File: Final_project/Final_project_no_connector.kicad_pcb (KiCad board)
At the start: 2 copper layers, 66 x 34.6 mm, 56 parts, among them J1 USB4105-GF-A, J2 Conn_01x04, J4 LEFT, J5 RIGHT, U1 RP2040, U2 MCP1702T-3302E_CB, U3 W25Q128JV, U4 ESP32-WROOM-32, U5 LM393D, Y1 12MHz

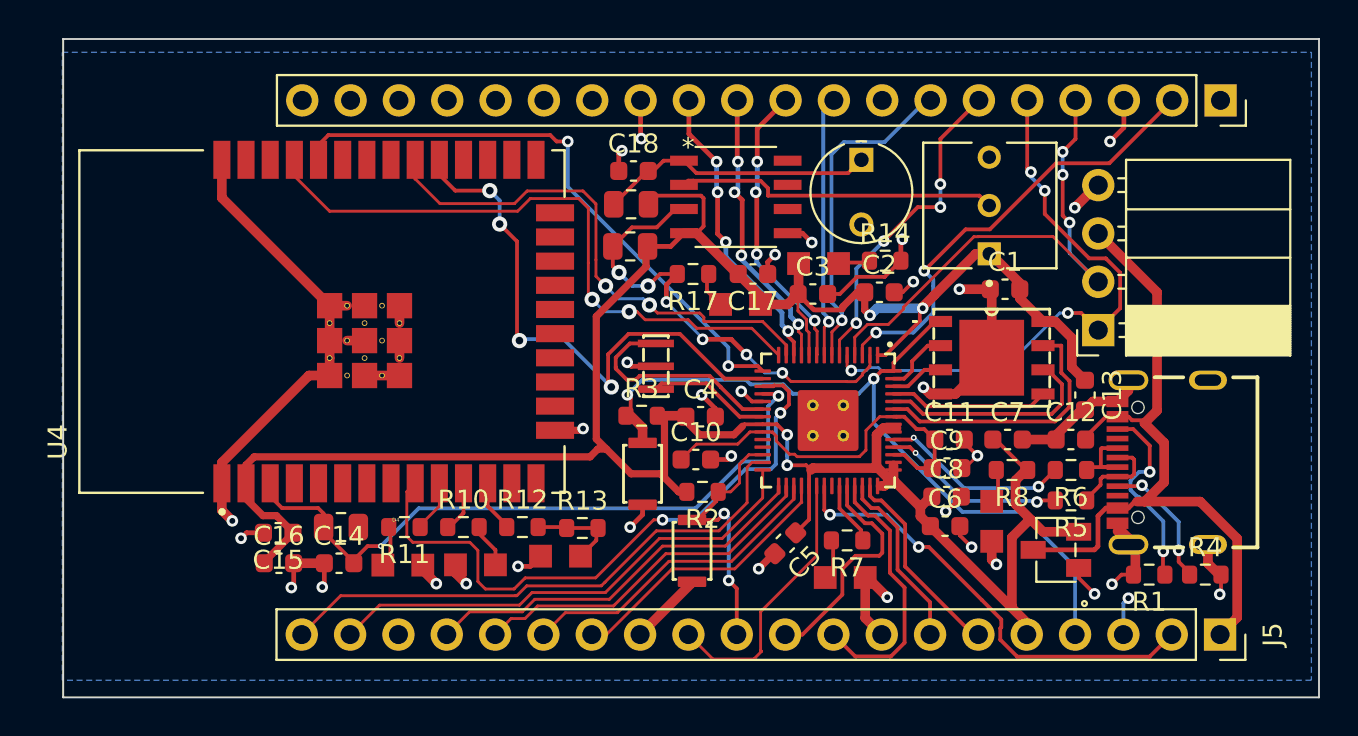
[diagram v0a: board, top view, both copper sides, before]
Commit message: Add final layout with no connector
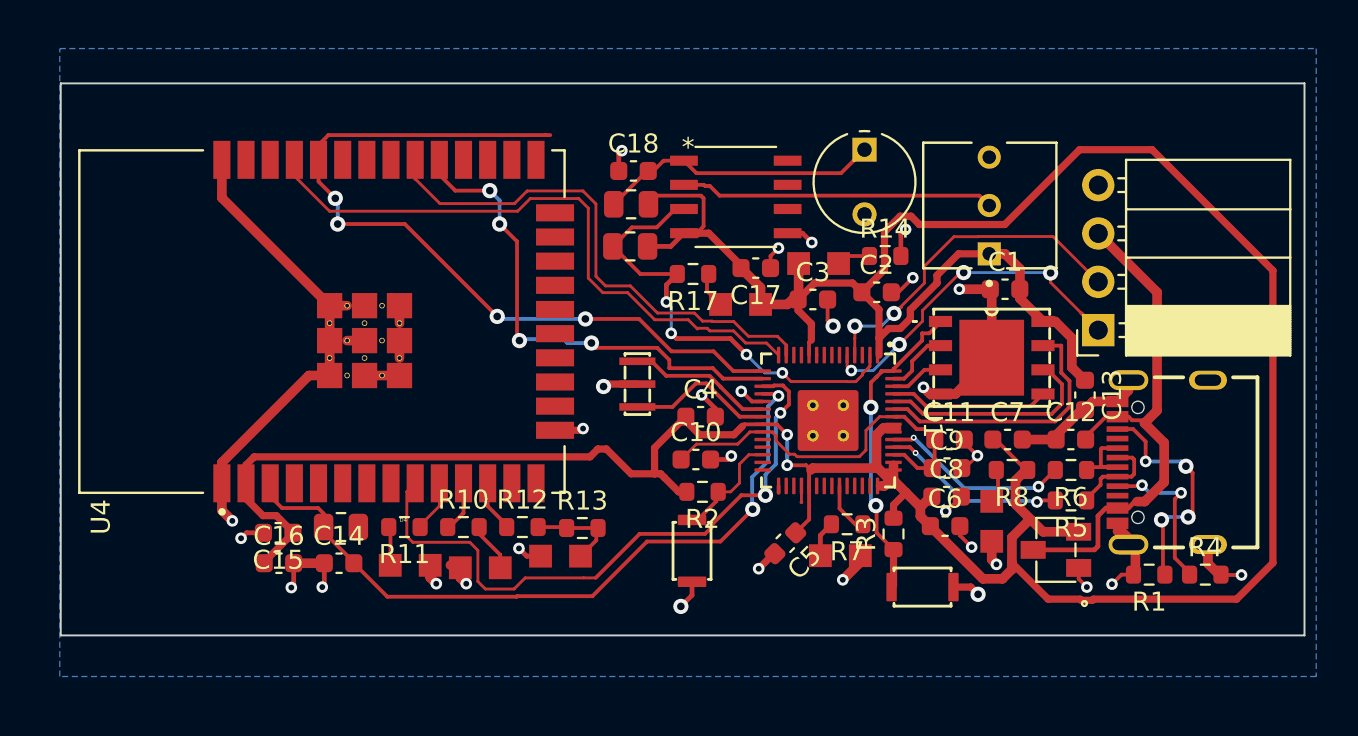
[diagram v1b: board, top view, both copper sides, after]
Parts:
- removed J4: LEFT, Connector_PinSocket_2.54mm:PinSocket_1x20_P2.54mm_Vertical
- removed J5: RIGHT, Connector_PinSocket_2.54mm:PinSocket_1x20_P2.54mm_Vertical
- moved S2 15.9 mm to (135.8, 89.2), turned to 180 degrees
- moved R3 14.6 mm to (134.2, 86.4), turned to 90 degrees
- moved Y1 1.35 mm to (120.8, 78.5)
- moved D1 1.18 mm to (131.4, 87.5)
- moved R7 0.85 mm to (131.8, 85.9)
- moved R18 0.56 mm to (132.7, 66.2)
- moved D4 0.39 mm to (108.8, 88.0)
- moved C17 0.34 mm to (127.0, 72.4)
- moved D3 0.30 mm to (112.5, 88.1)
- moved C3 0.29 mm to (130.0, 74.0)
- moved R14 0.25 mm to (133.8, 71.8)
- moved C2 0.15 mm to (133.3, 73.7)
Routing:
- net +3V3: track 143.0 -> 187.1 mm, vias 4 -> 2
- net /GPIO16: track 29.1 -> 0.00 mm
- net /GPIO17: track 26.1 -> 0.00 mm
- net /BOOT: track 41.4 -> 16.6 mm
- net /GPIO1: track 24.2 -> 0.00 mm, vias 2 -> 0
- net /GPIO23: track 23.9 -> 0.00 mm, vias 2 -> 0
- net /GPIO18: track 20.9 -> 0.36 mm
- net /GPIO19: track 18.8 -> 0.00 mm
- net /GPIO5: track 17.4 -> 0.00 mm, vias 1 -> 0
- net GND: track 109.8 -> 92.7 mm, vias 33 -> 31
- net /GPIO4: track 17.1 -> 0.00 mm, vias 4 -> 0
- net /GPIO20: track 16.8 -> 0.00 mm
- net /GPIO9: track 15.7 -> 0.00 mm, vias 4 -> 0
- net /GPIO7: track 15.4 -> 0.03 mm, vias 4 -> 0
- net /GPIO8: track 15.0 -> 0.00 mm, vias 4 -> 0
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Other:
- board size 66 x 34.6 mm -> 65.4 x 29 mm

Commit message: Clean layout and ESP32 footprint
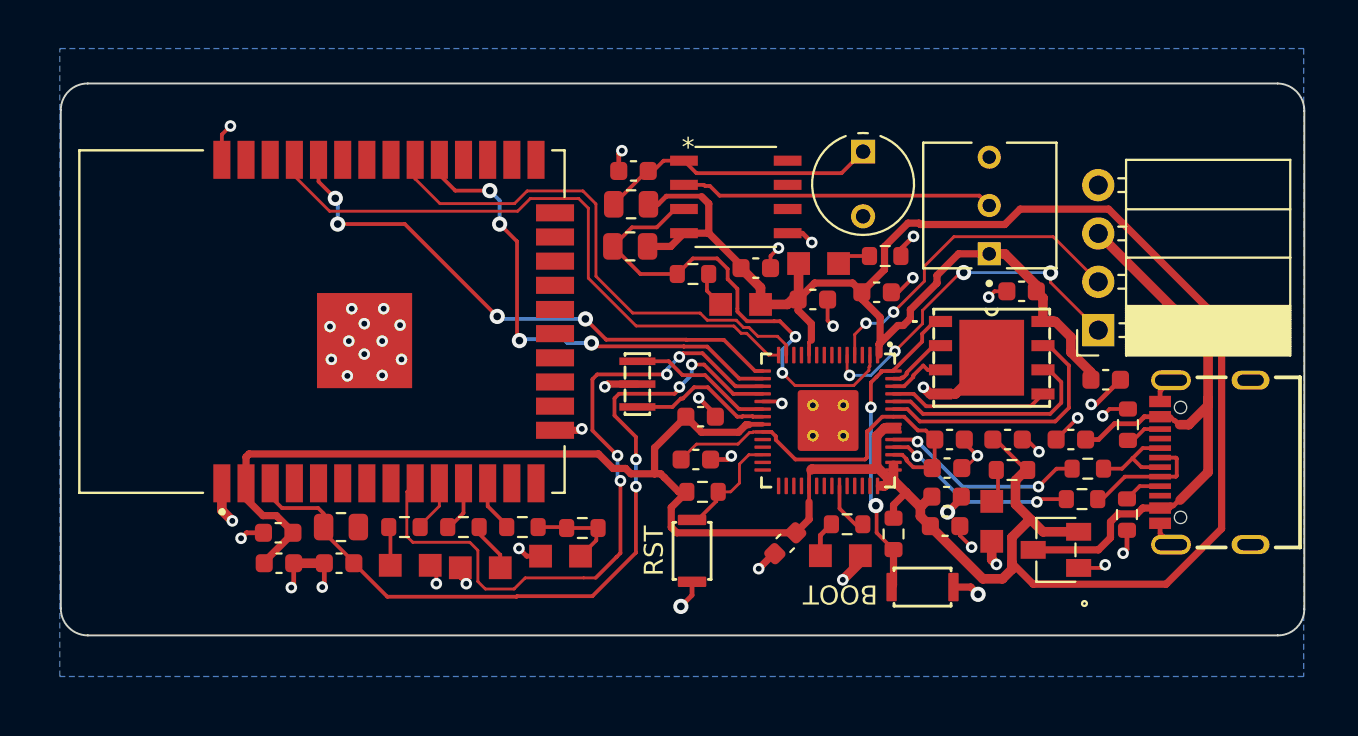
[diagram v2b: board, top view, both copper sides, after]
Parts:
- moved R1 7.96 mm to (146.6, 80.6), turned to 90 degrees
- moved R4 5.19 mm to (146.5, 85.3), turned to -90 degrees
- moved J1 2.24 mm to (153.0, 82.6)
- moved C13 1.35 mm to (145.4, 78.3), turned to 0 degrees
- moved R6 0.89 mm to (144.4, 82.9)
- moved C1 0.88 mm to (141.0, 73.6)
- moved R5 0.58 mm to (144.1, 84.5)
- moved R18 0.13 mm to (132.6, 66.3)
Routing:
- net GND: track 92.7 -> 57.0 mm, vias 31 -> 47
- net /GPIO12: track 42.5 -> 29.3 mm
- net Net-(J1-PadB5): track 12.5 -> 1.94 mm, vias 4 -> 0
- net +3V3: track 187.1 -> 177.5 mm, vias 2 -> 0
- net Net-(J1-PadA5): track 8.33 -> 2.02 mm, vias 2 -> 0
- net /VBUS: track 28.3 -> 34.3 mm
- net /GPIO14: track 33.6 -> 37.2 mm, vias 2 -> 4
- net /GPIO15: track 38.4 -> 41.8 mm, vias 2 -> 4
- net Net-(J1-PadA7): track 5.02 -> 6.46 mm
- net /GPIO21: track 0.86 -> 0.00 mm
- net /GPIO2: track 18.3 -> 17.5 mm
- net /GPIO0: track 25.6 -> 26.4 mm, vias 4 -> 2
- net /GPIO3: track 19.2 -> 18.4 mm
- net Net-(R6-Pad2): track 10.1 -> 10.8 mm
- net Net-(J1-PadA6): track 4.46 -> 5.06 mm
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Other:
- outline, holes or cut-outs redrawn
